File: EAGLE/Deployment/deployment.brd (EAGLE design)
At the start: 160 x 100 mm, 6 parts, among them Q1 100V 14A

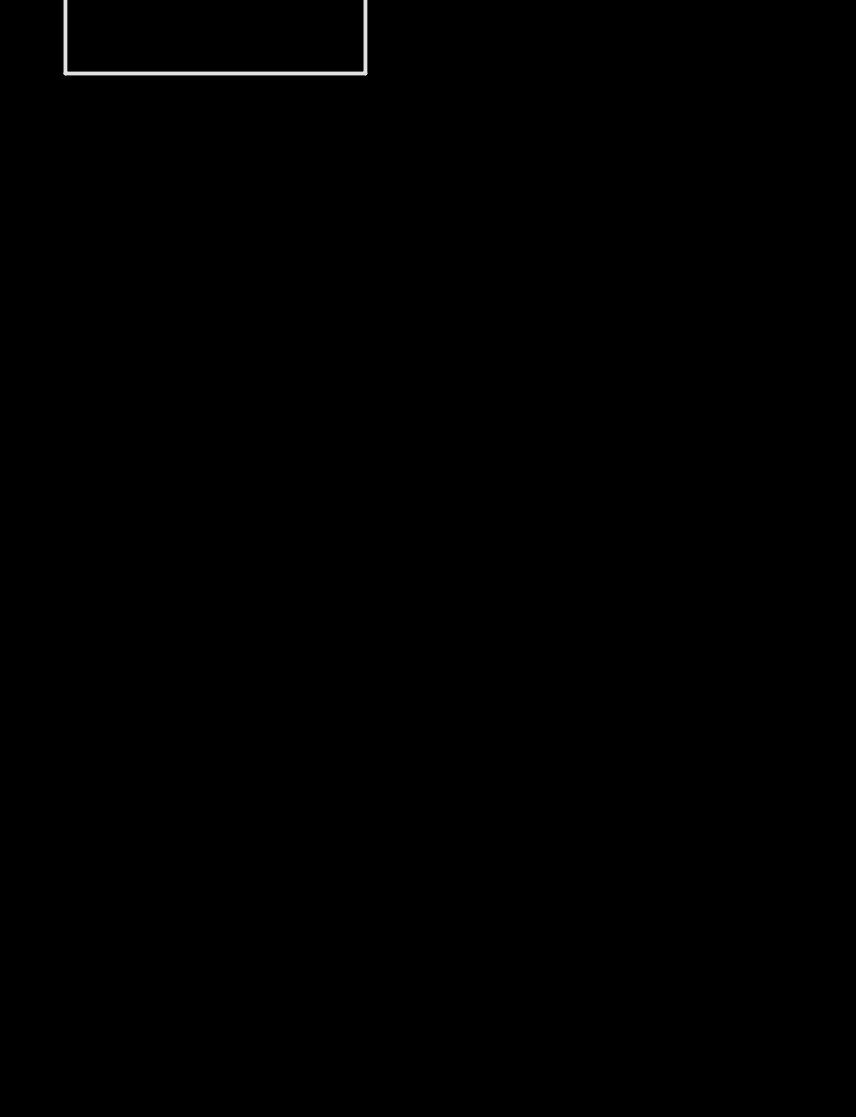
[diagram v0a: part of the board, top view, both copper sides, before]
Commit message: Fixed wiring of nichrome wire circit in the depolyment schematic
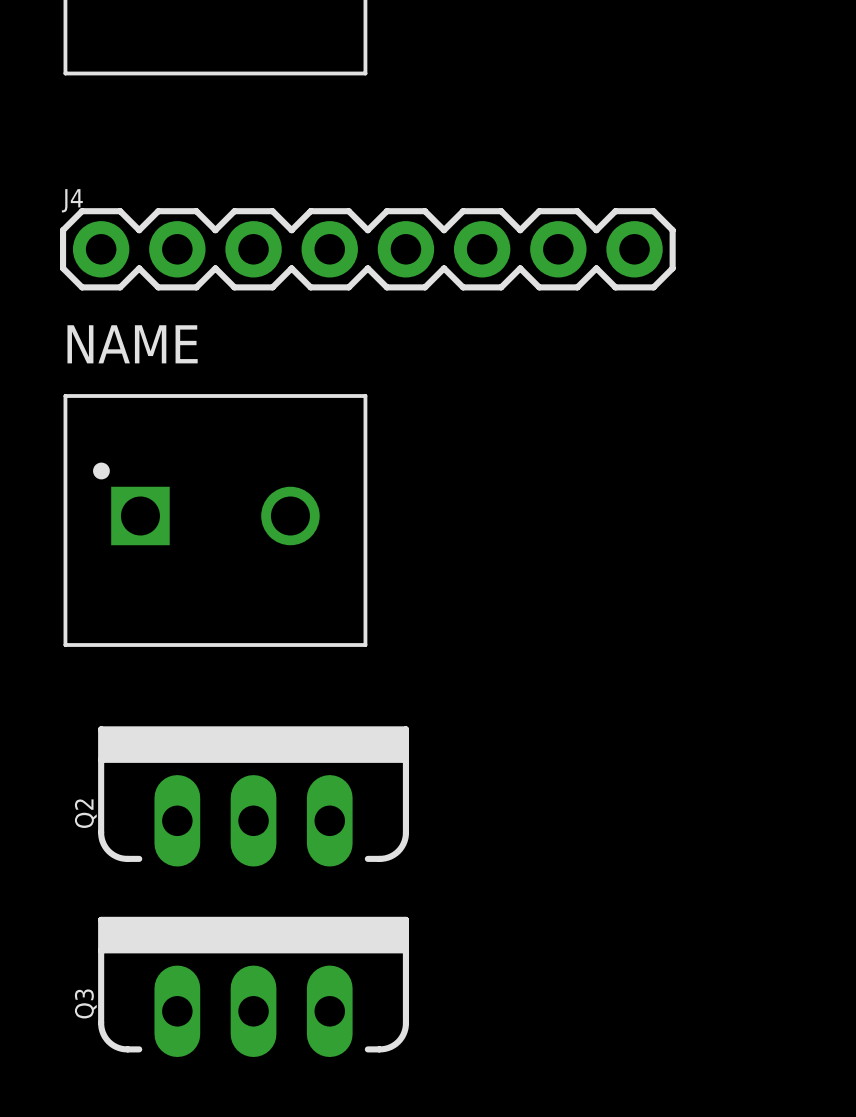
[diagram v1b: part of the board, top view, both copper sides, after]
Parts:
- added J4: (no value), SparkFun-Connectors:1X08
- added J5: (no value), 1935161:PHOENIX_1935161
- added Q2, Q3: 100V 14A, SparkFun-DiscreteSemi:TO220V
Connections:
- new net 4: Q3.1
- new net N$2: J5.1, Q2.3
- new net N$9: J4.8
- net +3V3: now also J4.7
- net 10: now also J4.1, J4.2
- net 3: now also Q2.1
- net 9V: now also J5.2
- net GND: now also J4.6, Q2.2
- net MISO: now also J4.4
- net MOSI: now also J4.3
- net SCK: now also J4.5
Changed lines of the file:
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@@
 <?xml version="1.0" encoding="utf-8"?>
 <!DOCTYPE eagle SYSTEM "eagle.dtd">
-<eagle version="9.5.2">
+<eagle version="9.2.2">
 <drawing>
 <settings>
@@
 <attribute name="PACKAGE" value="None" x="-59.69" y="-26.67" size="1.778" layer="27" display="off"/>
 </element>
+<element name="J4" library="SparkFun-Connectors" library_urn="urn:adsk.eagle:library:513" package="1X08" package3d_urn="urn:adsk.eagle:package:38138/1" value="" x="-52.07" y="-50.8" smashed="yes">
+<attribute name="NAME" x="-53.34" y="-49.403" size="0.6096" layer="25" font="vector" ratio="20"/>
+<attribute name="PROD_ID" value="CONN-08438" x="-52.07" y="-50.8" size="1.778" layer="27" display="off"/>
+<attribute name="VALUE" x="-53.34" y="-52.832" size="0.6096" layer="27" font="vector" ratio="20"/>
+</element>
+<element name="Q2" library="SparkFun-DiscreteSemi" library_urn="urn:adsk.eagle:library:514" package="TO220V" package3d_urn="urn:adsk.eagle:package:38447/1" value="100V 14A" x="-46.99" y="-69.85" smashed="yes">
+<attribute name="NAME" x="-52.324" y="-69.596" size="0.6096" layer="25" font="vector" ratio="20" rot="R90" align="bottom-center"/>
+<attribute name="PROD_ID" value="TRANS-10060" x="-46.99" y="-55.88" size="1.778" layer="27" display="off"/>
+<attribute name="VALUE" x="-41.656" y="-69.596" size="0.6096" layer="27" font="vector" ratio="20" rot="R90" align="top-center"/>
+</element>
+<element name="J5" library="1935161" package="PHOENIX_1935161" value="" x="-48.26" y="-59.69" smashed="yes">
+<attribute name="DESCRIPTION" value=" Conn Terminal Blocks 2 POS 5mm Solder ST Thru-Hole 16A " x="-59.69" y="-50.8" size="1.778" layer="27" display="off"/>
+<attribute name="DIGI-KEY_PART_NUMBER" value="277-1667-ND" x="-59.69" y="-50.8" size="1.778" layer="27" display="off"/>
+<attribute name="DIGI-KEY_PURCHASE_URL" value="https://www.digikey.com/product-detail/en/phoenix-contact/1935161/277-1667-ND/568614?utm_source=snapeda&amp;utm_medium=aggregator&amp;utm_campaign=symbol" x="-59.69" y="-50.8" size="1.778" layer="27" display="off"/>
+<attribute name="MF" value="Phoenix Contact" x="-59.69" y="-50.8" size="1.778" layer="27" display="off"/>
+<attribute name="MP" value="1935161" x="-59.69" y="-50.8" size="1.778" layer="27" display="off"/>
+<attribute name="PACKAGE" value="None" x="-59.69" y="-50.8" size="1.778" layer="27" display="off"/>
+</element>
+<element name="Q3" library="SparkFun-DiscreteSemi" library_urn="urn:adsk.eagle:library:514" package="TO220V" package3d_urn="urn:adsk.eagle:package:38447/1" value="100V 14A" x="-46.99" y="-76.2" smashed="yes">
+<attribute name="NAME" x="-52.324" y="-75.946" size="0.6096" layer="25" font="vector" ratio="20" rot="R90" align="bottom-center"/>
+<attribute name="PROD_ID" value="TRANS-10060" x="-46.99" y="-76.2" size="1.778" layer="27" display="off"/>
+<attribute name="VALUE" x="-41.656" y="-75.946" size="0.6096" layer="27" font="vector" ratio="20" rot="R90" align="top-center"/>
+</element>
 </elements>
 <signals>
@@
 <contactref element="J3" pad="2"/>
 <contactref element="Q1" pad="2"/>
+<contactref element="J4" pad="6"/>
+<contactref element="Q2" pad="2"/>
+<wire x1="-39.37" y1="-50.8" x2="-46.99" y2="-69.85" width="0" layer="19" extent="1-1"/>
+<wire x1="-45.76" y1="-40.64" x2="-39.37" y2="-50.8" width="0" layer="19" extent="1-1"/>
 <wire x1="-46.99" y1="-3.81" x2="-45.76" y2="-40.64" width="0" layer="19" extent="1-1"/>
 <wire x1="-21.59" y1="1.27" x2="-46.99" y2="-3.81" width="0" layer="19" extent="1-1"/>
@@
 <signal name="MOSI">
 <contactref element="JP1" pad="5"/>
+<contactref element="J4" pad="3"/>
+<wire x1="-41.91" y1="1.27" x2="-46.99" y2="-50.8" width="0" layer="19" extent="1-1"/>
 </signal>
 <signal name="MISO">
 <contactref element="JP1" pad="4"/>
+<contactref element="J4" pad="4"/>
+<wire x1="-44.45" y1="1.27" x2="-44.45" y2="-50.8" width="0" layer="19" extent="1-1"/>
 </signal>
 <signal name="SCK">
 <contactref element="JP1" pad="6"/>
+<contactref element="J4" pad="5"/>
+<wire x1="-39.37" y1="1.27" x2="-41.91" y2="-50.8" width="0" layer="19" extent="1-1"/>
 </signal>
 <signal name="RST">
@@
 <signal name="10">
 <contactref element="JP3" pad="7"/>
+<contactref element="J4" pad="1"/>
+<contactref element="J4" pad="2"/>
+<wire x1="-49.53" y1="-50.8" x2="-52.07" y2="-50.8" width="0" layer="19" extent="1-1"/>
+<wire x1="-26.67" y1="6.35" x2="-49.53" y2="-50.8" width="0" layer="19" extent="1-1"/>
 </signal>
 <signal name="6">
@@
 <signal name="+3V3">
 <contactref element="JP1" pad="15"/>
+<contactref element="J4" pad="7"/>
+<wire x1="-16.51" y1="1.27" x2="-36.83" y2="-50.8" width="0" layer="19" extent="1-1"/>
 </signal>
 <signal name="VBUS">
@@
 <signal name="3">
 <contactref element="JP3" pad="11"/>
+<contactref element="Q2" pad="1"/>
+<wire x1="-16.51" y1="6.35" x2="-49.53" y2="-69.85" width="0" layer="19" extent="1-1"/>
 </signal>
 <signal name="EN">
@@
 <contactref element="J1" pad="2"/>
 <contactref element="J2" pad="1"/>
+<contactref element="J5" pad="2"/>
+<wire x1="-50.76" y1="-26.67" x2="-45.76" y2="-59.69" width="0" layer="19" extent="1-1"/>
 <wire x1="-45.76" y1="-12.7" x2="-50.76" y2="-26.67" width="0" layer="19" extent="1-1"/>
 </signal>
@@
 <wire x1="-45.76" y1="-26.67" x2="-50.76" y2="-40.64" width="0" layer="19" extent="1-1"/>
 </signal>
+<signal name="N$9">
+<contactref element="J4" pad="8"/>
+</signal>
+<signal name="N$2">
+<contactref element="J5" pad="1"/>
+<contactref element="Q2" pad="3"/>
+<wire x1="-50.76" y1="-59.69" x2="-44.45" y2="-69.85" width="0" layer="19" extent="1-1"/>
+</signal>
+<signal name="4">
+<contactref element="Q3" pad="1"/>
+</signal>
 </signals>

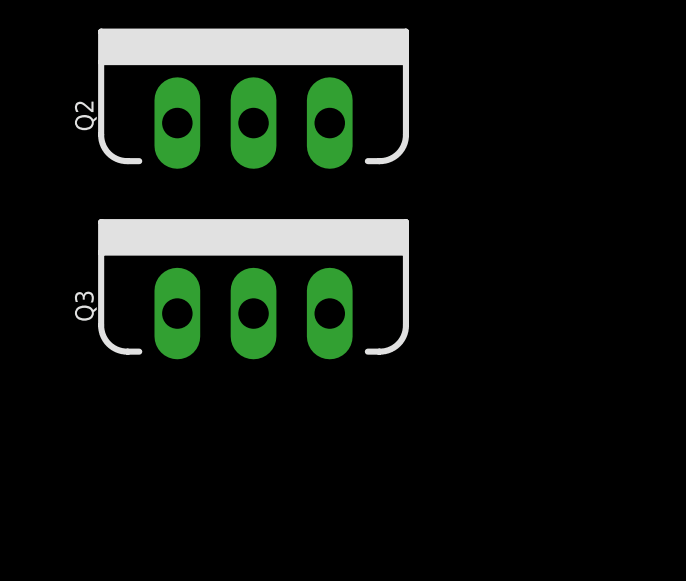
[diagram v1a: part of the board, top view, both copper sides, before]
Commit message: Fixed issue with buzzer wiring
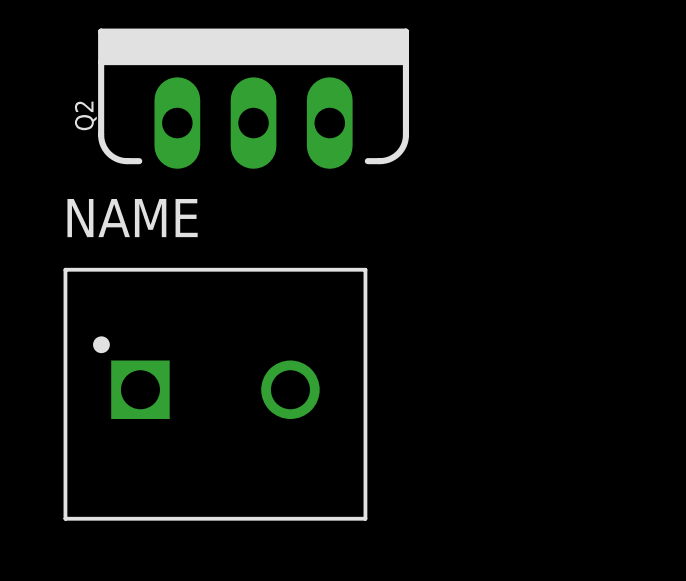
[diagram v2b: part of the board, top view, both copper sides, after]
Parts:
- removed Q3: 100V 14A, SparkFun-DiscreteSemi:TO220V
- added J6: (no value), 1935161:PHOENIX_1935161
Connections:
- removed net 4: Q3.1
- net 9V: now also J6.2
- net GND: now also J6.1
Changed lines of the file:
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@@
 <attribute name="PACKAGE" value="None" x="-59.69" y="-50.8" size="1.778" layer="27" display="off"/>
 </element>
-<element name="Q3" library="SparkFun-DiscreteSemi" library_urn="urn:adsk.eagle:library:514" package="TO220V" package3d_urn="urn:adsk.eagle:package:38447/1" value="100V 14A" x="-46.99" y="-76.2" smashed="yes">
-<attribute name="NAME" x="-52.324" y="-75.946" size="0.6096" layer="25" font="vector" ratio="20" rot="R90" align="bottom-center"/>
-<attribute name="PROD_ID" value="TRANS-10060" x="-46.99" y="-76.2" size="1.778" layer="27" display="off"/>
-<attribute name="VALUE" x="-41.656" y="-75.946" size="0.6096" layer="27" font="vector" ratio="20" rot="R90" align="top-center"/>
+<element name="J6" library="1935161" package="PHOENIX_1935161" value="" x="-48.26" y="-78.74" smashed="yes">
+<attribute name="DESCRIPTION" value=" Conn Terminal Blocks 2 POS 5mm Solder ST Thru-Hole 16A " x="-59.69" y="-64.77" size="1.778" layer="27" display="off"/>
+<attribute name="DIGI-KEY_PART_NUMBER" value="277-1667-ND" x="-59.69" y="-64.77" size="1.778" layer="27" display="off"/>
+<attribute name="DIGI-KEY_PURCHASE_URL" value="https://www.digikey.com/product-detail/en/phoenix-contact/1935161/277-1667-ND/568614?utm_source=snapeda&amp;utm_medium=aggregator&amp;utm_campaign=symbol" x="-59.69" y="-64.77" size="1.778" layer="27" display="off"/>
+<attribute name="MF" value="Phoenix Contact" x="-59.69" y="-64.77" size="1.778" layer="27" display="off"/>
+<attribute name="MP" value="1935161" x="-59.69" y="-64.77" size="1.778" layer="27" display="off"/>
+<attribute name="PACKAGE" value="None" x="-59.69" y="-64.77" size="1.778" layer="27" display="off"/>
 </element>
 </elements>
@@
 <contactref element="J4" pad="6"/>
 <contactref element="Q2" pad="2"/>
+<contactref element="J6" pad="1"/>
+<wire x1="-46.99" y1="-69.85" x2="-50.76" y2="-78.74" width="0" layer="19" extent="1-1"/>
 <wire x1="-39.37" y1="-50.8" x2="-46.99" y2="-69.85" width="0" layer="19" extent="1-1"/>
 <wire x1="-45.76" y1="-40.64" x2="-39.37" y2="-50.8" width="0" layer="19" extent="1-1"/>
@@
 <contactref element="J2" pad="1"/>
 <contactref element="J5" pad="2"/>
+<contactref element="J6" pad="2"/>
+<wire x1="-45.76" y1="-59.69" x2="-45.76" y2="-78.74" width="0" layer="19" extent="1-1"/>
 <wire x1="-50.76" y1="-26.67" x2="-45.76" y2="-59.69" width="0" layer="19" extent="1-1"/>
 <wire x1="-45.76" y1="-12.7" x2="-50.76" y2="-26.67" width="0" layer="19" extent="1-1"/>
@@
 <wire x1="-50.76" y1="-59.69" x2="-44.45" y2="-69.85" width="0" layer="19" extent="1-1"/>
 </signal>
-<signal name="4">
-<contactref element="Q3" pad="1"/>
-</signal>
 </signals>
